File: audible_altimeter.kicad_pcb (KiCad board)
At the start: 2 copper layers, 52 x 29 mm, 54 parts, among them CON1 BUQ2-USB-MICRO-B, IC1 BUQ2-ATXMEGA128A4U-A, P1 CONN_2, Q1 NPN, U1 MCP7940M, U10 CNT, U11 DWN, U13 FLASH_MEMORY, U2 MCP73831-SOT-23-5, U3 NCP4681-SC-70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

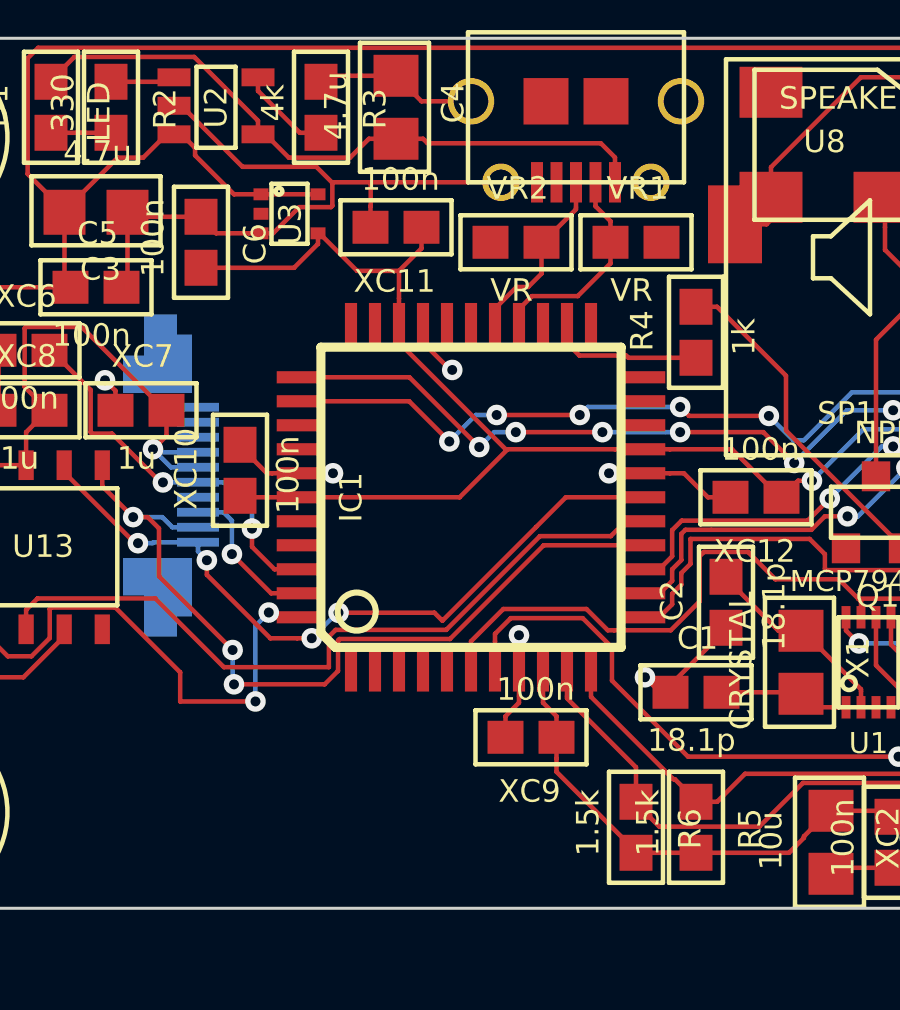
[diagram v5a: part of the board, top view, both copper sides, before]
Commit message: Add new barometer
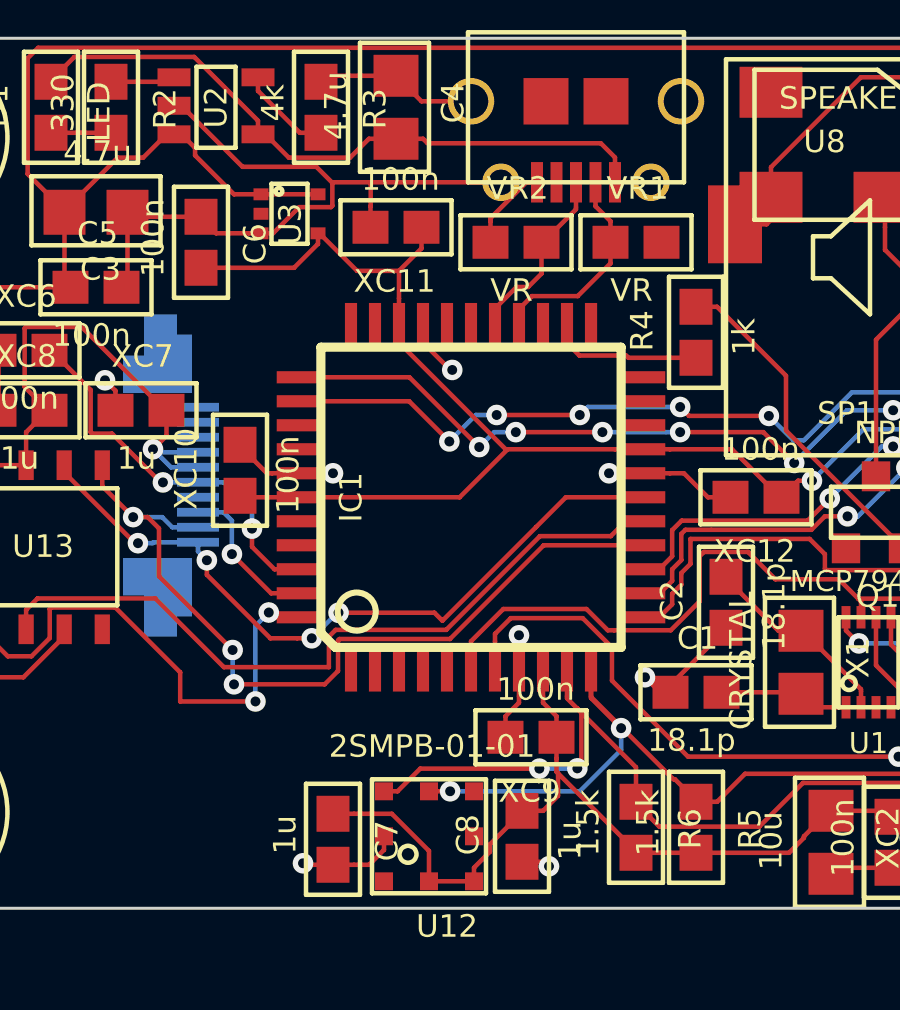
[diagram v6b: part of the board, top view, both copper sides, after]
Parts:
- added C7: 1u, buq2:SM0603, F.Cu at (152.9, 122.9)
- added C8: 1u, buq2:SM0603, F.Cu at (159.2, 122.8)
- added U12: 2SMPB-01-01, buq2:2SMPB-01-01, F.Cu at (156.1, 122.8)
- moved LS013B7DH03-FPC 13.7 mm to (148.7, 151.9)
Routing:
- net /Battery/+3.3V: track 145.9 -> 157.3 mm
- net /Barometer/I2C_SCL: track 35.5 -> 45.6 mm, vias 0 -> 2
- net /Barometer/I2C_SDA: track 61.7 -> 70.6 mm, vias 2 -> 4
- net GND: track 67.3 -> 74.5 mm, vias 15 -> 17

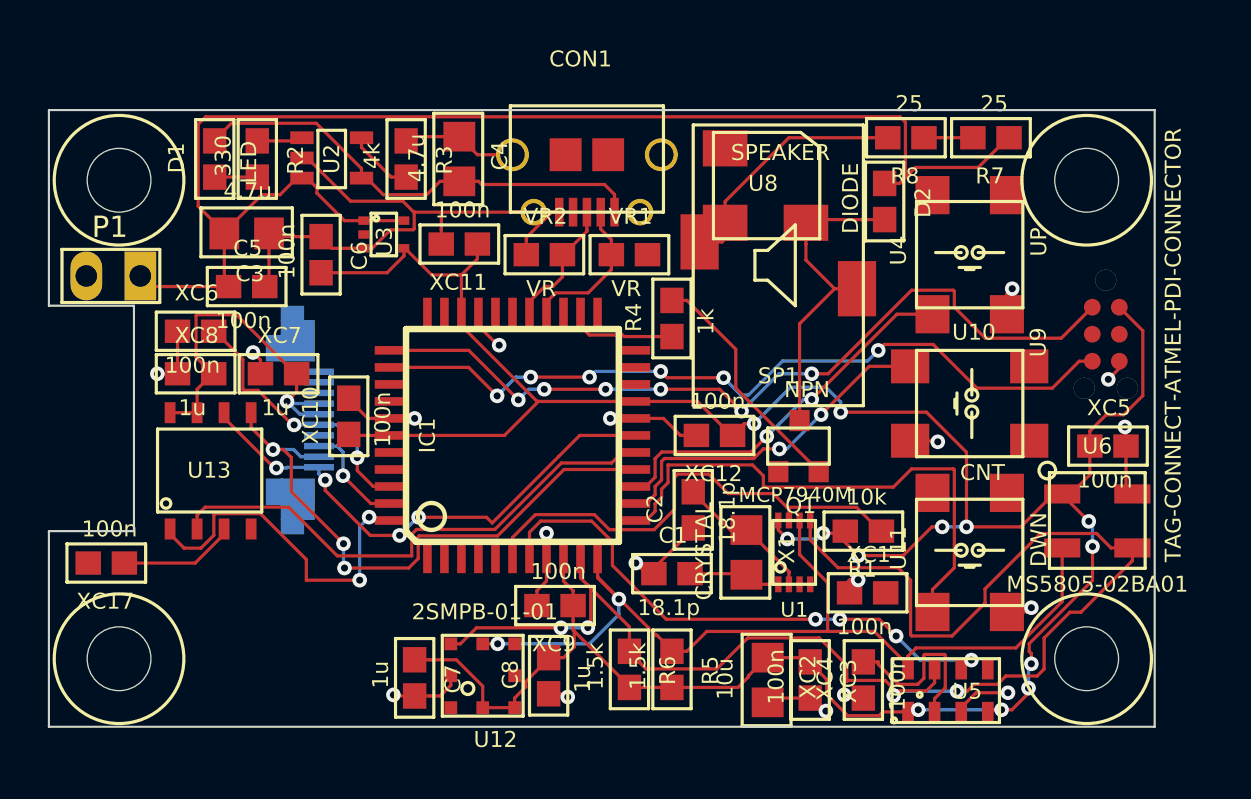
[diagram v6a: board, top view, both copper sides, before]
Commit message: Ordered version 2.0 (pcb and stencil)
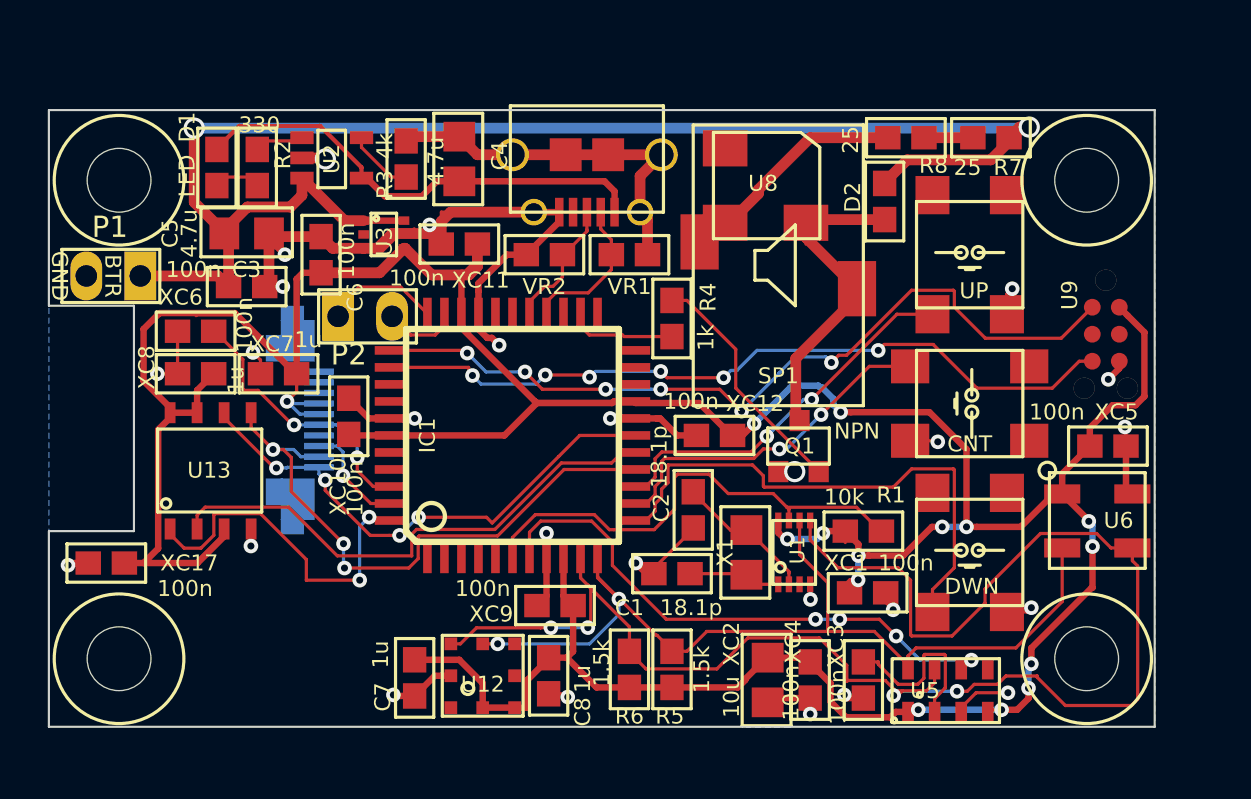
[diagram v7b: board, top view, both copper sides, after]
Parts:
- added P2: SERIAL, buq2:PIN_HEADER_2, F.Cu at (149.3, 105.9)
- moved LS013B7DH03-FPC 7.16 mm to (144.0, 146.5)
- moved D1 0.41 mm to (143.6, 98.9)
- moved R2 0.40 mm to (145.5, 98.9)
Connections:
- IC1 pad 32: (no net) -> Net-(IC1-Pad32)
- IC1 pad 33: (no net) -> Net-(IC1-Pad33)
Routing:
- net /Battery/+3.3V: track 157.3 -> 199.9 mm
- net GND: track 74.5 -> 101.4 mm, vias 17 -> 26
- net /Battery/BATTERY: track 66.3 -> 76.6 mm, vias 0 -> 2
- net Net-(IC1-Pad33): track 0.00 -> 5.53 mm
- net /Barometer/I2C_SDA: track 70.6 -> 75.1 mm
- net Net-(IC1-Pad32): track 0.00 -> 3.56 mm
- net Net-(D2-Pad1): track 15.4 -> 16.3 mm
- net /MCU/PDI_CLK: track 36.8 -> 35.9 mm
- net Net-(R8-Pad1): track 11.9 -> 11.0 mm
- added copper zone on B.Cu, net GND
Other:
- board text added: "AudibleA V2.0 Matti Jukola 2015-01-27"
- board text added: "BTR"
- board text added: "GND"
- board text added: "RX"
- board text added: "TX"

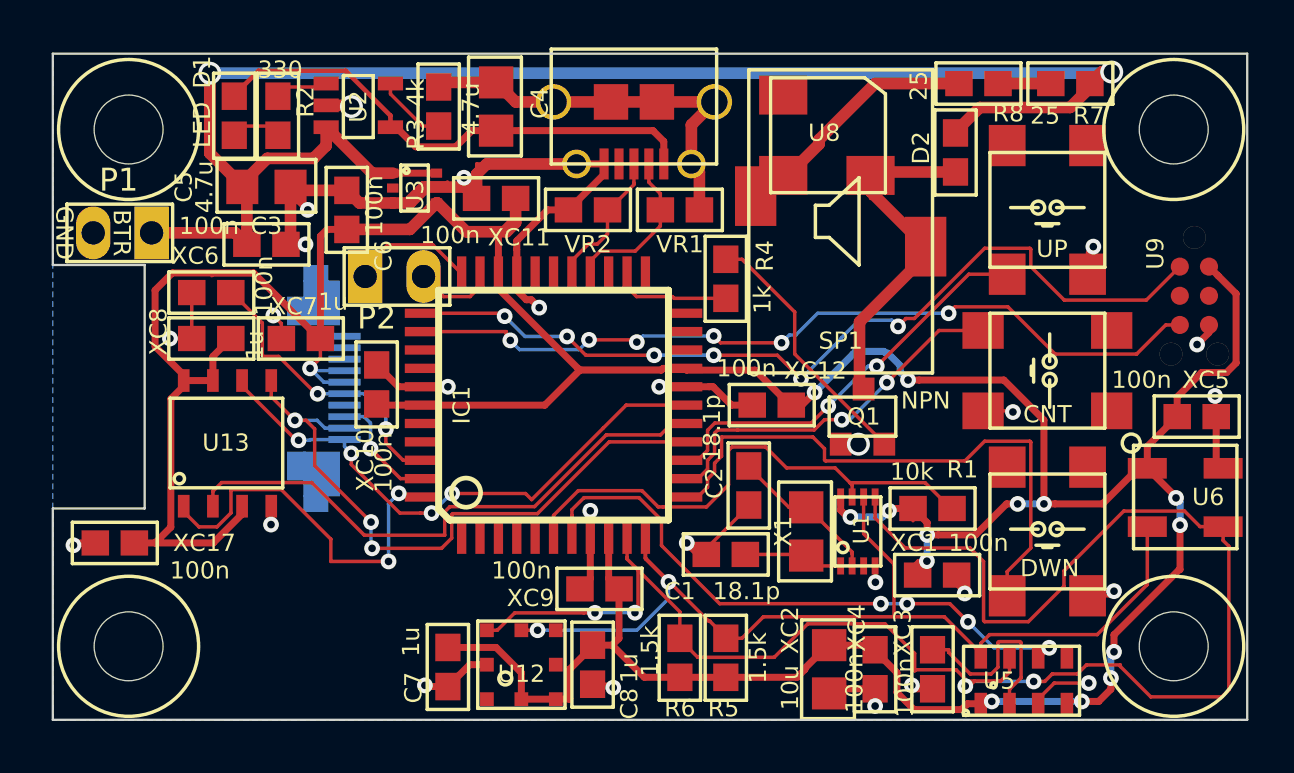
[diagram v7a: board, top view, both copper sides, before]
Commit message: Start implementing new version: move USB port and altimeter module, new buzzer and volume control
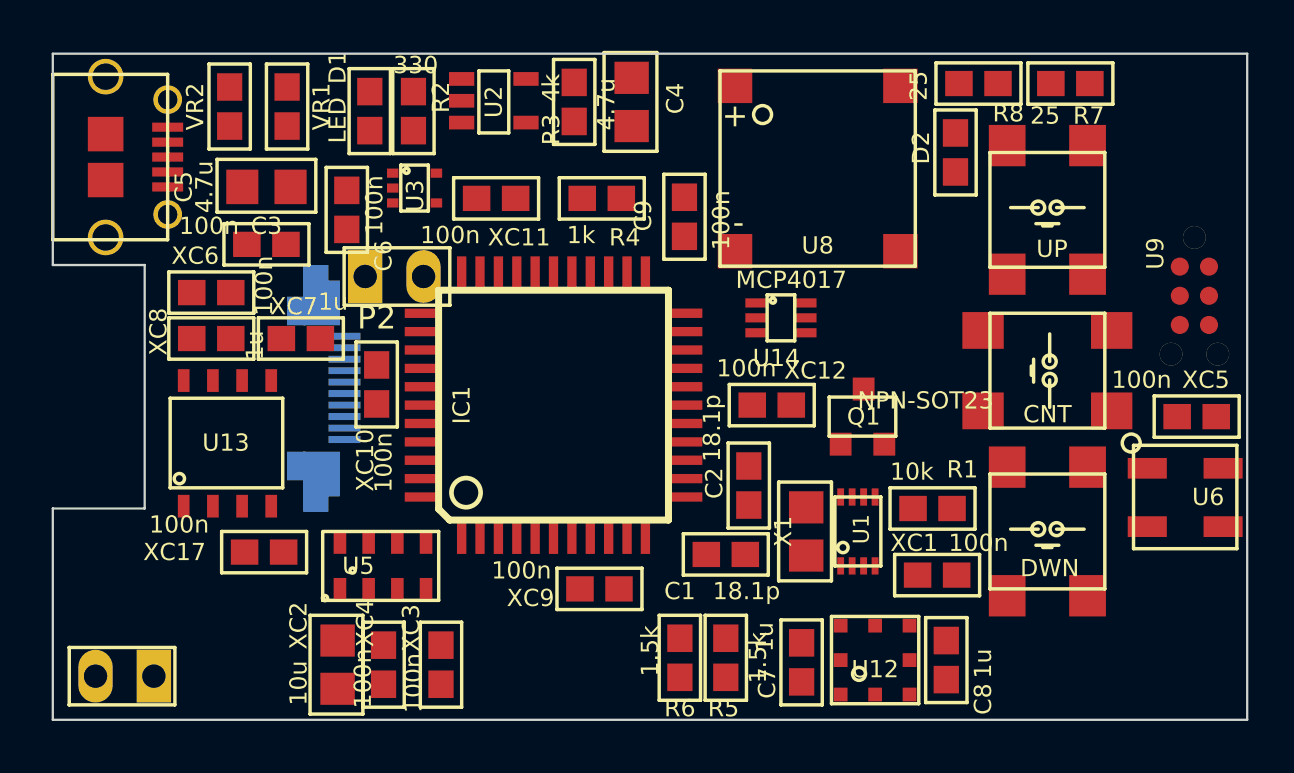
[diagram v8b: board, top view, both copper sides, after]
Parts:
- removed LS013B7DH03-FPC: VAL**, buq2:LS013B7DH03-FPC
- removed MOUNTING_HOLE (x4): VAL**, buq2:MOUNTING_HOLE
- removed SP1: SPEAKER, buq2:SPEAKER_240326000031
- added C9: 100n, buq2:SM0603, F.Cu at (163.2, 103.3)
- added U14: MCP4017, buq2:SC-70-6, F.Cu at (167.4, 107.7)
- Q1: value NPN -> NPN-SOT23
- U8: value CSS-0575A-SMT -> SPEAKER-WITH-DUMMY; footprint buq2:BUZZER-CUI-5MM -> buq2:SPEAKER-T0825TR
- moved U5 28.3 mm to (150.1, 118.5)
- moved XC2 21.4 mm to (148.1, 122.8)
- moved XC3 21.4 mm to (150.1, 122.8)
- moved XC4 21.4 mm to (152.6, 122.8)
- moved CON1 20.3 mm to (140.7, 100.7), turned to 270 degrees
- moved P1 19.3 mm to (140.1, 123.3)
- moved VR1 17.7 mm to (145.9, 98.5), turned to 270 degrees
- moved VR2 16.2 mm to (143.4, 98.5), turned to 90 degrees
- moved C7 15.4 mm to (168.3, 122.7)
- moved C8 15.4 mm to (174.6, 122.6)
- moved U12 15.4 mm to (171.5, 122.6)
- moved XC17 6.51 mm to (144.9, 117.9), turned to 180 degrees
- moved R4 6.44 mm to (159.6, 102.5), turned to 180 degrees
- moved C4 5.90 mm to (160.9, 98.3)
- moved D1 5.90 mm to (149.5, 98.7)
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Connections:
- IC1 pad 1: (no net) -> /Buttons/BUTTON_DOWN
- IC1 pad 12: /Buttons/BUTTON_DOWN -> (no net)
- IC1 pad 13: /Buttons/BUTTON_CENTER -> (no net)
- IC1 pad 14: /Buttons/BUTTON_UP -> (no net)
- IC1 pad 2: (no net) -> /Buttons/BUTTON_CENTER
- IC1 pad 24: /Buzzer/BUZZER_DRIVE -> (no net)
- IC1 pad 3: (no net) -> /Buttons/BUTTON_UP
- P1 pad 1: /Battery/BATTERY -> GND
- P1 pad 2: GND -> /Battery/BATTERY
- Q1 pad 1: GND -> Net-(Q1-Pad1)
- Q1 pad 2: Net-(Q1-Pad2) -> GND
- R4 pad 1: Net-(Q1-Pad2) -> Net-(Q1-Pad1)
- R4 pad 2: /Buzzer/BUZZER_DRIVE -> Net-(R4-Pad2)
- U8 pad 3: (no net) -> Net-(U8-Pad3)
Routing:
- net /Battery/+3.3V: track 199.9 -> 0.00 mm, vias 15 -> 0
- net GND: track 101.4 -> 0.00 mm, vias 26 -> 0
- net /Battery/BATTERY: track 76.6 -> 0.00 mm, vias 2 -> 0
- net /Barometer/I2C_SDA: track 75.1 -> 0.00 mm, vias 4 -> 0
- net /Barometer/I2C_SCL: track 45.6 -> 0.00 mm, vias 2 -> 0
- net /MCU/PDI_DATA: track 38.9 -> 0.00 mm, vias 6 -> 0
- net /MCU/PDI_CLK: track 35.9 -> 0.00 mm, vias 6 -> 0
- net /Display/MOSI: track 28.1 -> 0.00 mm, vias 3 -> 0
- net /MCU/BAROMETER_INT: track 26.2 -> 0.00 mm, vias 4 -> 0
- net /Buttons/BUTTON_DOWN: track 25.3 -> 0.00 mm
- net /MCU/MISO: track 25.2 -> 0.00 mm
- net /MCU/SCK: track 24.5 -> 0.00 mm, vias 4 -> 0
- net /MCU/CLOCK_INT: track 22.7 -> 0.00 mm
- net /Battery/+5V: track 22.4 -> 0.00 mm
- net /Buttons/BUTTON_UP: track 17.9 -> 0.00 mm, vias 2 -> 0
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- removed copper zone on B.Cu, net GND
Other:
- board text removed: "BTR"
- board text removed: "GND"
